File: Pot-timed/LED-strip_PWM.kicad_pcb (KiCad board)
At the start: 2 copper layers, 29.7 x 10 mm, 16 parts, among them IC1 MADW__ATTINY13-MM, P1 CONN_2, P2 CONN_2, T1 AO3400, U1 MCP1804-SOT23-5

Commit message: Pot-timed (s.b.): added alternative MOSFET to schematic + Rev. update.
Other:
- board text added: "V0.12.a POT PWM controller"
- board text removed: "V0.12 POT PWM controller"
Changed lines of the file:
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@@
-(kicad_pcb (version 3) (host pcbnew "(2013-07-05 BZR 4237)-testing")
+(kicad_pcb (version 3) (host pcbnew "(2013-07-14 BZR 4242)-testing")
   (general
     (links 31)
@@
     (title LED-strip_PWM)
     (date "24 May 2013")
-    (rev 0.12)
+    (rev 0.12.a)
     (company "2012 - blog.spitzenpfeil.org")
   )
@@
     (arrow2b (pts (xy 76 59.3) (xy 77.126504 58.713579)))
   )
-  (gr_text "V0.12\nPOT PWM controller" (at 91 53.2) (layer B.SilkS)
+  (gr_text "V0.12.a\nPOT PWM controller" (at 91 53.2) (layer B.SilkS)
     (effects (font (size 1 1) (thickness 0.2032)) (justify mirror))
   )

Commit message: Pot-timed (s.b.): added info helpful for panelization.
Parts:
- added mouse-bite-1mm: VAL**, MADW__mouse-bite-1mm-slot, F.Cu at (79.5, 47.4)
- added mouse-bite-1mm: VAL**, MADW__mouse-bite-1mm-slot, F.Cu at (79.5, 58.6)
- added mouse-bite-1mm: VAL**, MADW__mouse-bite-1mm-slot, F.Cu at (101.8, 47.4)
- added mouse-bite-1mm: VAL**, MADW__mouse-bite-1mm-slot, F.Cu at (101.8, 58.6)
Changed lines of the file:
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@@
-(kicad_pcb (version 3) (host pcbnew "(2013-07-14 BZR 4242)-testing")
+(kicad_pcb (version 3) (host pcbnew "(2013-08-08 BZR 4279)-product")
   (general
     (links 31)
     (no_connects 0)
-    (area 74.5076 46.7476 111.616669 61.100001)
+    (area 71.419823 44.6476 111.616669 61.4524)
     (thickness 1.6002)
-    (drawings 18)
+    (drawings 34)
     (tracks 168)
     (zones 0)
-    (modules 16)
+    (modules 20)
     (nets 15)
   )
@@
     (22 B.Mask user)
     (23 F.Mask user)
+    (24 Dwgs.User user)
     (25 Cmts.User user)
+    (26 Eco1.User user)
     (28 Edge.Cuts user)
   )
@@
     (zone_45_only yes)
     (trace_min 0.1524)
-    (segment_width 0.2)
+    (segment_width 1)
     (edge_width 0.2)
     (via_size 0.762)
@@
     (tags CAPACITOR)
     (attr smd)
-    (fp_text reference C1 (at 3.1 -0.6 180) (layer F.SilkS)
+    (fp_text reference C1 (at 3.1 -0.15 180) (layer F.SilkS)
       (effects (font (size 0.8 0.8) (thickness 0.2)))
     )
@@
       (xy -0.90932 1.3462)) (layer B.SilkS) (width 0.00254))
   )
+  (module MADW__mouse-bite-1mm-slot (layer Front)
+    (at 79.45 47.4)
+    (fp_text reference mouse-bite-1mm (at 0 -2) (layer F.SilkS) hide
+      (effects (font (size 1 1) (thickness 0.2)))
+    )
+    (fp_text value VAL** (at 0 2.1) (layer F.SilkS) hide
+      (effects (font (size 1 1) (thickness 0.2)))
+    )
+    (fp_arc (start 1.5 0) (end 1.1 0) (angle 90) (layer F.SilkS) (width 0.2))
+    (fp_arc (start 1.5 0) (end 1.5 0.4) (angle 90) (layer F.SilkS) (width 0.2))
+    (fp_arc (start -1.5 0) (end -1.5 -0.4) (angle 90) (layer F.SilkS) (width 0.2))
+    (fp_arc (start -1.5 0) (end -1.1 0) (angle 90) (layer F.SilkS) (width 0.2))
+    (fp_line (start -1.5 0) (end -1.5 0) (layer Eco1.User) (width 1))
+    (fp_line (start 1.5 0) (end 1.5 0) (layer Eco1.User) (width 1))
+    (pad "" np_thru_hole circle (at 0.35 -1) (size 0.5 0.5) (drill 0.5)
+      (layers *.Cu *.Mask F.SilkS)
+    )
+    (pad "" np_thru_hole circle (at -1.15 0.75) (size 0.5 0.5) (drill 0.5)
+      (layers *.Cu *.Mask F.SilkS)
+    )
+    (pad "" np_thru_hole circle (at 1.15 0.75) (size 0.5 0.5) (drill 0.5)
+      (layers *.Cu *.Mask F.SilkS)
+    )
+    (pad "" np_thru_hole circle (at -1.15 -0.75) (size 0.5 0.5) (drill 0.5)
+      (layers *.Cu *.Mask F.SilkS)
+    )
+    (pad "" np_thru_hole circle (at -0.35 -1) (size 0.5 0.5) (drill 0.5)
+      (layers *.Cu *.Mask F.SilkS)
+    )
+    (pad "" np_thru_hole circle (at 1.15 -0.75) (size 0.5 0.5) (drill 0.5)
+      (layers *.Cu *.Mask F.SilkS)
+    )
+    (pad "" np_thru_hole circle (at -0.35 1) (size 0.5 0.5) (drill 0.5)
+      (layers *.Cu *.Mask F.SilkS)
+    )
+    (pad "" np_thru_hole circle (at 0.35 1) (size 0.5 0.5) (drill 0.5)
+      (layers *.Cu *.Mask F.SilkS)
+    )
+  )
+  (module MADW__mouse-bite-1mm-slot (layer Front)
+    (at 79.45 58.6)
+    (fp_text reference mouse-bite-1mm (at 0 -2) (layer F.SilkS) hide
+      (effects (font (size 1 1) (thickness 0.2)))
+    )
+    (fp_text value VAL** (at 0 2.1) (layer F.SilkS) hide
+      (effects (font (size 1 1) (thickness 0.2)))
+    )
+    (fp_arc (start 1.5 0) (end 1.1 0) (angle 90) (layer F.SilkS) (width 0.2))
+    (fp_arc (start 1.5 0) (end 1.5 0.4) (angle 90) (layer F.SilkS) (width 0.2))
+    (fp_arc (start -1.5 0) (end -1.5 -0.4) (angle 90) (layer F.SilkS) (width 0.2))
+    (fp_arc (start -1.5 0) (end -1.1 0) (angle 90) (layer F.SilkS) (width 0.2))
+    (fp_line (start -1.5 0) (end -1.5 0) (layer Eco1.User) (width 1))
+    (fp_line (start 1.5 0) (end 1.5 0) (layer Eco1.User) (width 1))
+    (pad "" np_thru_hole circle (at 0.35 -1) (size 0.5 0.5) (drill 0.5)
+      (layers *.Cu *.Mask F.SilkS)
+    )
+    (pad "" np_thru_hole circle (at -1.15 0.75) (size 0.5 0.5) (drill 0.5)
+      (layers *.Cu *.Mask F.SilkS)
+    )
+    (pad "" np_thru_hole circle (at 1.15 0.75) (size 0.5 0.5) (drill 0.5)
+      (layers *.Cu *.Mask F.SilkS)
+    )
+    (pad "" np_thru_hole circle (at -1.15 -0.75) (size 0.5 0.5) (drill 0.5)
+      (layers *.Cu *.Mask F.SilkS)
+    )
+    (pad "" np_thru_hole circle (at -0.35 -1) (size 0.5 0.5) (drill 0.5)
+      (layers *.Cu *.Mask F.SilkS)
+    )
+    (pad "" np_thru_hole circle (at 1.15 -0.75) (size 0.5 0.5) (drill 0.5)
+      (layers *.Cu *.Mask F.SilkS)
+    )
+    (pad "" np_thru_hole circle (at -0.35 1) (size 0.5 0.5) (drill 0.5)
+      (layers *.Cu *.Mask F.SilkS)
+    )
+    (pad "" np_thru_hole circle (at 0.35 1) (size 0.5 0.5) (drill 0.5)
+      (layers *.Cu *.Mask F.SilkS)
+    )
+  )
+  (module MADW__mouse-bite-1mm-slot (layer Front)
+    (at 101.8 47.4)
+    (fp_text reference mouse-bite-1mm (at 0 -2) (layer F.SilkS) hide
+      (effects (font (size 1 1) (thickness 0.2)))
+    )
+    (fp_text value VAL** (at 0 2.1) (layer F.SilkS) hide
+      (effects (font (size 1 1) (thickness 0.2)))
+    )
+    (fp_arc (start 1.5 0) (end 1.1 0) (angle 90) (layer F.SilkS) (width 0.2))
+    (fp_arc (start 1.5 0) (end 1.5 0.4) (angle 90) (layer F.SilkS) (width 0.2))
+    (fp_arc (start -1.5 0) (end -1.5 -0.4) (angle 90) (layer F.SilkS) (width 0.2))
+    (fp_arc (start -1.5 0) (end -1.1 0) (angle 90) (layer F.SilkS) (width 0.2))
+    (fp_line (start -1.5 0) (end -1.5 0) (layer Eco1.User) (width 1))
+    (fp_line (start 1.5 0) (end 1.5 0) (layer Eco1.User) (width 1))
+    (pad "" np_thru_hole circle (at 0.35 -1) (size 0.5 0.5) (drill 0.5)
+      (layers *.Cu *.Mask F.SilkS)
+    )
+    (pad "" np_thru_hole circle (at -1.15 0.75) (size 0.5 0.5) (drill 0.5)
+      (layers *.Cu *.Mask F.SilkS)
+    )
+    (pad "" np_thru_hole circle (at 1.15 0.75) (size 0.5 0.5) (drill 0.5)
+      (layers *.Cu *.Mask F.SilkS)
+    )
+    (pad "" np_thru_hole circle (at -1.15 -0.75) (size 0.5 0.5) (drill 0.5)
+      (layers *.Cu *.Mask F.SilkS)
+    )
+    (pad "" np_thru_hole circle (at -0.35 -1) (size 0.5 0.5) (drill 0.5)
+      (layers *.Cu *.Mask F.SilkS)
+    )
+    (pad "" np_thru_hole circle (at 1.15 -0.75) (size 0.5 0.5) (drill 0.5)
+      (layers *.Cu *.Mask F.SilkS)
+    )
+    (pad "" np_thru_hole circle (at -0.35 1) (size 0.5 0.5) (drill 0.5)
+      (layers *.Cu *.Mask F.SilkS)
+    )
+    (pad "" np_thru_hole circle (at 0.35 1) (size 0.5 0.5) (drill 0.5)
+      (layers *.Cu *.Mask F.SilkS)
+    )
+  )
+  (module MADW__mouse-bite-1mm-slot (layer Front)
+    (at 101.8 58.6)
+    (fp_text reference mouse-bite-1mm (at 0 -2) (layer F.SilkS) hide
+      (effects (font (size 1 1) (thickness 0.2)))
+    )
+    (fp_text value VAL** (at 0 2.1) (layer F.SilkS) hide
+      (effects (font (size 1 1) (thickness 0.2)))
+    )
+    (fp_arc (start 1.5 0) (end 1.1 0) (angle 90) (layer F.SilkS) (width 0.2))
+    (fp_arc (start 1.5 0) (end 1.5 0.4) (angle 90) (layer F.SilkS) (width 0.2))
+    (fp_arc (start -1.5 0) (end -1.5 -0.4) (angle 90) (layer F.SilkS) (width 0.2))
+    (fp_arc (start -1.5 0) (end -1.1 0) (angle 90) (layer F.SilkS) (width 0.2))
+    (fp_line (start -1.5 0) (end -1.5 0) (layer Eco1.User) (width 1))
+    (fp_line (start 1.5 0) (end 1.5 0) (layer Eco1.User) (width 1))
+    (pad "" np_thru_hole circle (at 0.35 -1) (size 0.5 0.5) (drill 0.5)
+      (layers *.Cu *.Mask F.SilkS)
+    )
+    (pad "" np_thru_hole circle (at -1.15 0.75) (size 0.5 0.5) (drill 0.5)
+      (layers *.Cu *.Mask F.SilkS)
+    )
+    (pad "" np_thru_hole circle (at 1.15 0.75) (size 0.5 0.5) (drill 0.5)
+      (layers *.Cu *.Mask F.SilkS)
+    )
+    (pad "" np_thru_hole circle (at -1.15 -0.75) (size 0.5 0.5) (drill 0.5)
+      (layers *.Cu *.Mask F.SilkS)
+    )
+    (pad "" np_thru_hole circle (at -0.35 -1) (size 0.5 0.5) (drill 0.5)
+      (layers *.Cu *.Mask F.SilkS)
+    )
+    (pad "" np_thru_hole circle (at 1.15 -0.75) (size 0.5 0.5) (drill 0.5)
+      (layers *.Cu *.Mask F.SilkS)
+    )
+    (pad "" np_thru_hole circle (at -0.35 1) (size 0.5 0.5) (drill 0.5)
+      (layers *.Cu *.Mask F.SilkS)
+    )
+    (pad "" np_thru_hole circle (at 0.35 1) (size 0.5 0.5) (drill 0.5)
+      (layers *.Cu *.Mask F.SilkS)
+    )
+  )
+  (gr_line (start 103.3 47.4) (end 104.65 47.4) (angle 90) (layer Eco1.User) (width 1))
+  (gr_line (start 106.25 57) (end 106.25 49) (angle 90) (layer Eco1.User) (width 1))
+  (gr_line (start 103.3 58.6) (end 104.65 58.6) (angle 90) (layer Eco1.User) (width 1))
+  (gr_line (start 80.95 58.6) (end 100.3 58.6) (angle 90) (layer Eco1.User) (width 1))
+  (gr_line (start 80.95 47.4) (end 100.3 47.4) (angle 90) (layer Eco1.User) (width 1))
+  (gr_line (start 75.4 49) (end 75.4 57) (angle 90) (layer Eco1.User) (width 1))
+  (gr_line (start 77.95 58.6) (end 77 58.6) (angle 90) (layer Eco1.User) (width 1))
+  (gr_line (start 77.95 47.4) (end 77 47.4) (angle 90) (layer Eco1.User) (width 1))
+  (gr_arc (start 77 49) (end 75.4 49) (angle 90) (layer Eco1.User) (width 1))
+  (gr_arc (start 77 57) (end 77 58.6) (angle 90) (layer Eco1.User) (width 1))
+  (gr_circle (center 77 57) (end 77.05 57) (layer Dwgs.User) (width 0.05))
+  (gr_circle (center 77 49) (end 77.05 49) (layer Dwgs.User) (width 0.05))
+  (gr_arc (start 104.65 57) (end 106.25 57) (angle 90) (layer Eco1.User) (width 1))
+  (gr_circle (center 104.65 57) (end 104.7 57) (layer Dwgs.User) (width 0.05))
+  (gr_arc (start 104.65 49) (end 104.65 47.4) (angle 90) (layer Eco1.User) (width 1))
+  (gr_circle (center 104.65 49) (end 104.7 49) (layer Dwgs.User) (width 0.05))
   (gr_line (start 76 57) (end 76 49) (angle 90) (layer Edge.Cuts) (width 0.2))
   (gr_line (start 104.65 58) (end 77 58) (angle 90) (layer Edge.Cuts) (width 0.2))

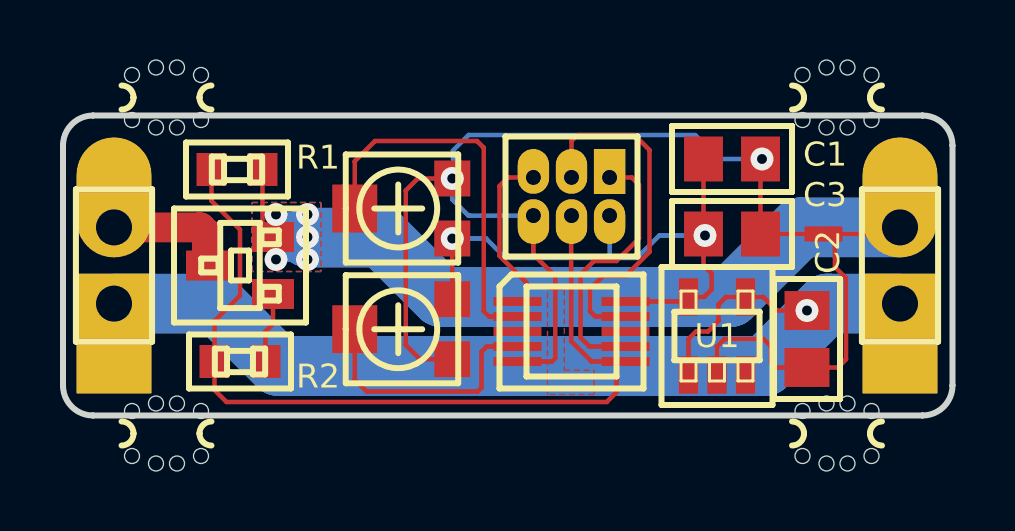
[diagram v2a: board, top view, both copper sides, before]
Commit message: Replaced MCP1804 with AP2204K-3.3TRG1 [TS5205CX533].
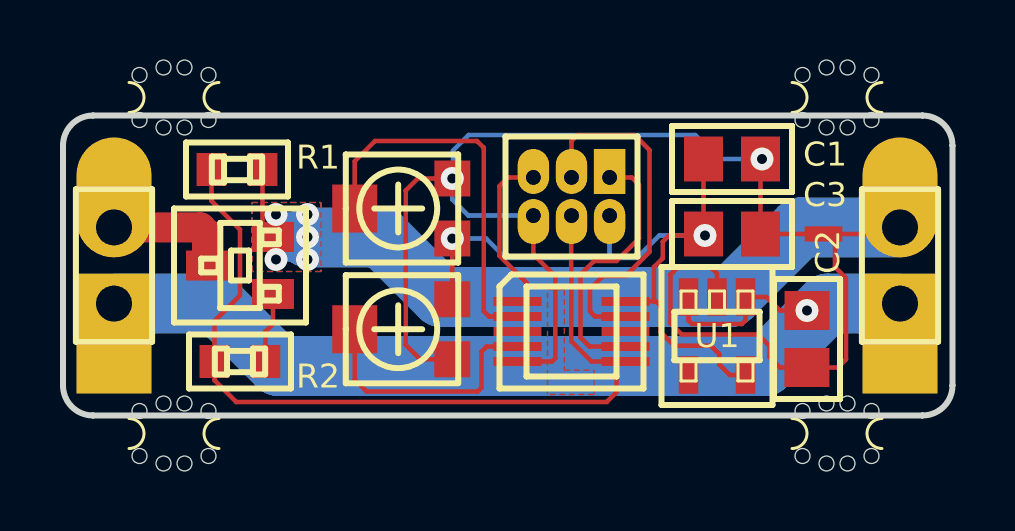
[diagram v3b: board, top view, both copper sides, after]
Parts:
- U1: value MCP1804-SOT23-5 -> AP2204K-3.3TRG1
- mouse-bite-1mm (x4): footprint MADW__mouse-bite-1mm-slot -> Panelization:mouse-bite-1mm-slot
- moved mouse-bite-1mm 0.25 mm to (79.7, 47.4)
- moved mouse-bite-1mm 0.25 mm to (79.7, 58.6)
- turned U1 to 180 degrees
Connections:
- IC1 pad 3: N-000005 -> (no net)
- IC1 pad 8: N-000006 -> (no net)
- U1 pad 3: (no net) -> /Vin
- U1 pad 4: /Vin -> (no net)
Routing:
- net GNDPWR: track 42.1 -> 46.9 mm
- net VCC: track 20.5 -> 24.9 mm
- net /Vin: track 38.0 -> 36.9 mm
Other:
- board text added: "2015 - blog.spitzenpfeil.org"
- board text added: "V0.13.a POT PWM controller"
- board text removed: "2013 - blog.spitzenpfeil.org"
- board text removed: "V0.12.a POT PWM controller"
